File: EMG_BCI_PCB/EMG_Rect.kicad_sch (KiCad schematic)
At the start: 24 parts, among them U3D ADA4807-4, U4A ADA4807-4, U4B ADA4807-4, U4C ADA4807-4, U4D ADA4807-4, U4E ADA4807-4

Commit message: More schematic changes
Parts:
- removed TP6: TestPoint, Connector_PinHeader_2.54mm:PinHeader_1x01_P2.54mm_Vertical, symbol Connector:TestPoint
- removed U4C, U4D: ADA4807-4, Package_SO:TSSOP-14_4.4x5mm_P0.65mm, symbol EMG_Circuit:ADA4807-4
- added C5, C7: 4.7uF, Capacitor_SMD:C_0603_1608Metric_Pad1.05x0.95mm_HandSolder, symbol Device:C
- added R4, R5, R6: 10k, Resistor_SMD:R_0805_2012Metric_Pad1.15x1.40mm_HandSolder, symbol Device:R
- added unit 4 of U4
- added U8: MCP1501-18xCH, Package_TO_SOT_SMD:SOT-23-6, symbol Reference_Voltage:MCP1501-18xCH
- renumbered U4E to U4, U3D to U4, U4A to U4, U4B to U4
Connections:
- net +5V: now also C5.2, U8.4 (~{SHDN}), U8.6 (VDD)
- net Earth: now also C5.1, C7.1, U4.12 (+), U8.2 (GND), U8.3 (GND), U8.5 (GND)
- net LP_IN: now also U4.2 (-), R4.2; no longer U4.13 (-)
- net RectSignalAdc: now reaches C18.1, R17.1, TP5.1
- net at RV2.1, TP4.1: now also R17.2, U4.8; no longer U4.7
- net at R13.1, RV2.2: now also U4.9 (-); no longer U4.6 (-)
- net at R16.1, TP3.1: now also U4.10 (+), U4.7; no longer U4.1, U4.5 (+)
- net at C17.2, D1.1 (K), D2.2 (A): now also U4.1; no longer U4.14
- net at C17.1, D1.2 (A), R14.2: now also U4.3 (+); no longer U4.12 (+)
- net at D2.1 (K), R15.2: now also U4.6 (-); no longer U4.2 (-)
- net at R14.1, R16.2: now also U4.5 (+); no longer U4.3 (+)
- new net: C7.2, R6.2, U8.1 (OUT)
- new net: R4.1, R5.2, R6.1, U4.13 (-)
- new net RawSignalAdc: R5.1, U4.14
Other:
- moved on the sheet: C18, R17, TP5

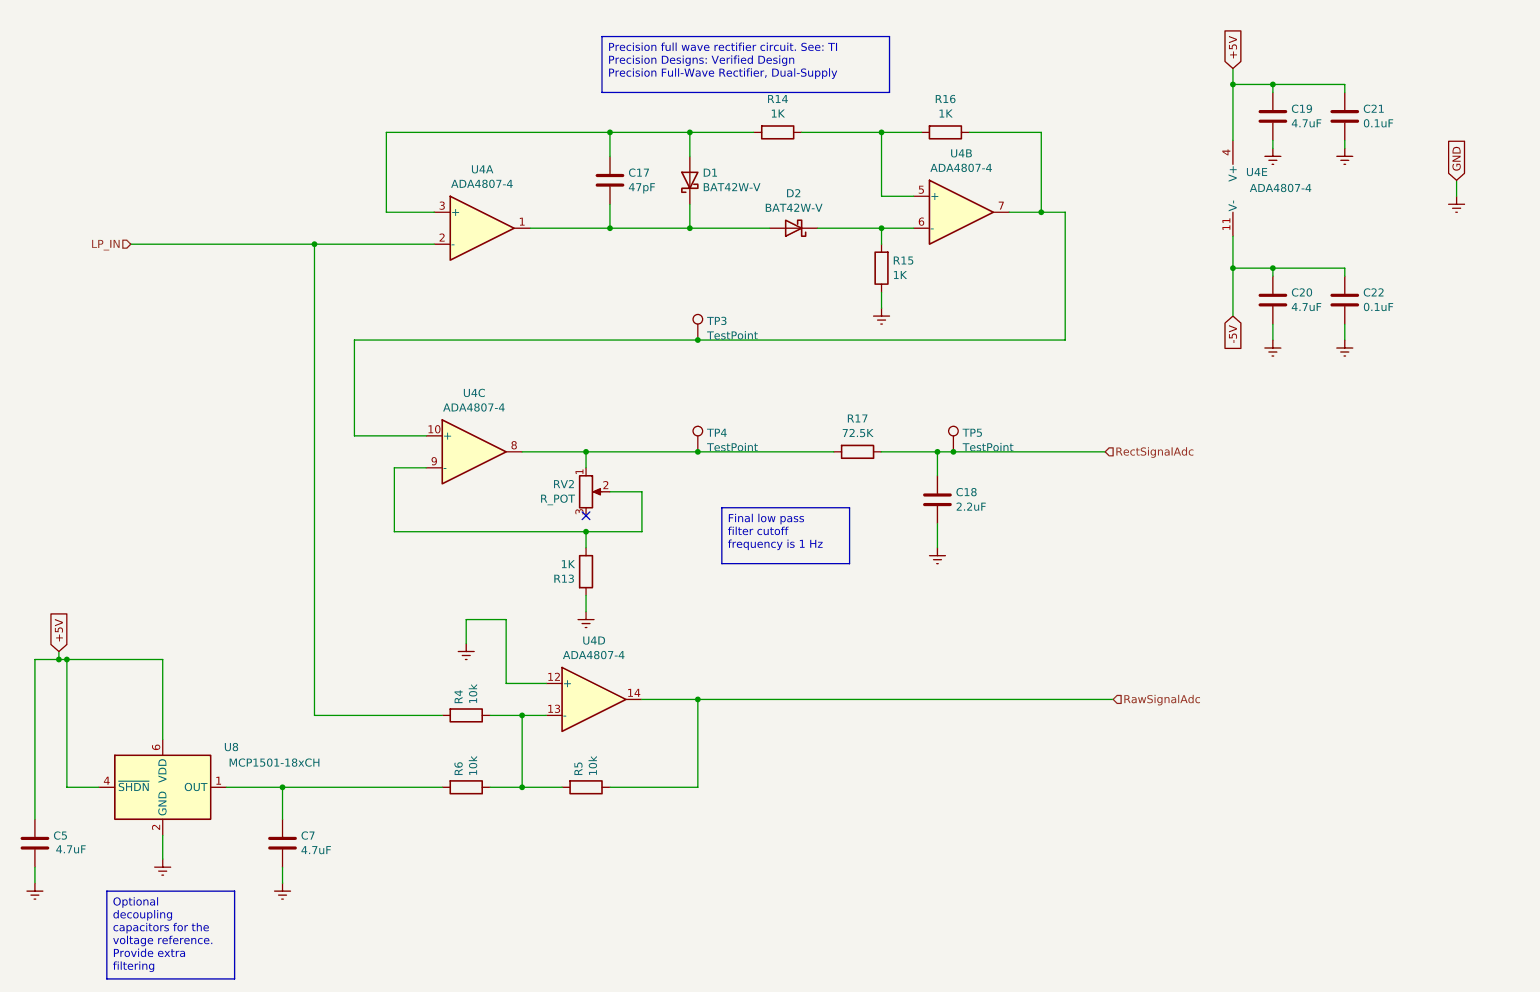
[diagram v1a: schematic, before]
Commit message: Added power symbols for +/-3.3V
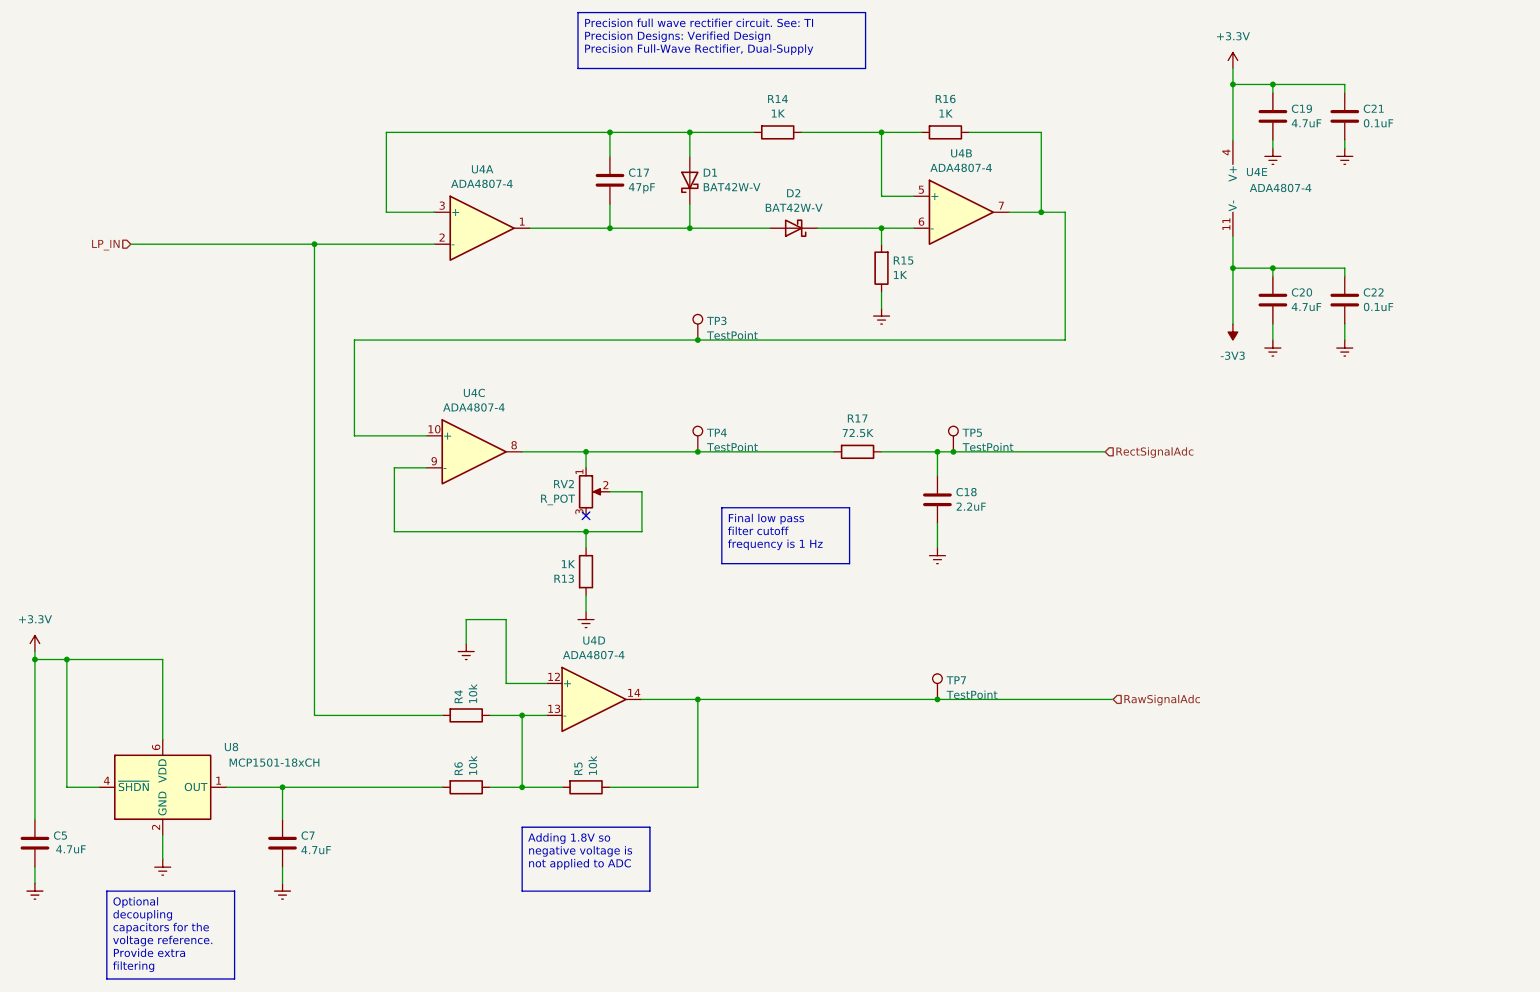
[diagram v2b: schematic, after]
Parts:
- added TP7: TestPoint, Connector_PinHeader_2.54mm:PinHeader_1x01_P2.54mm_Vertical, symbol Connector:TestPoint
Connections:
- net RawSignalAdc: now also TP7.1
- net +5V renamed +3.3V
- net -5V renamed -3V3

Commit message: Removed some warnings from the electrical rules
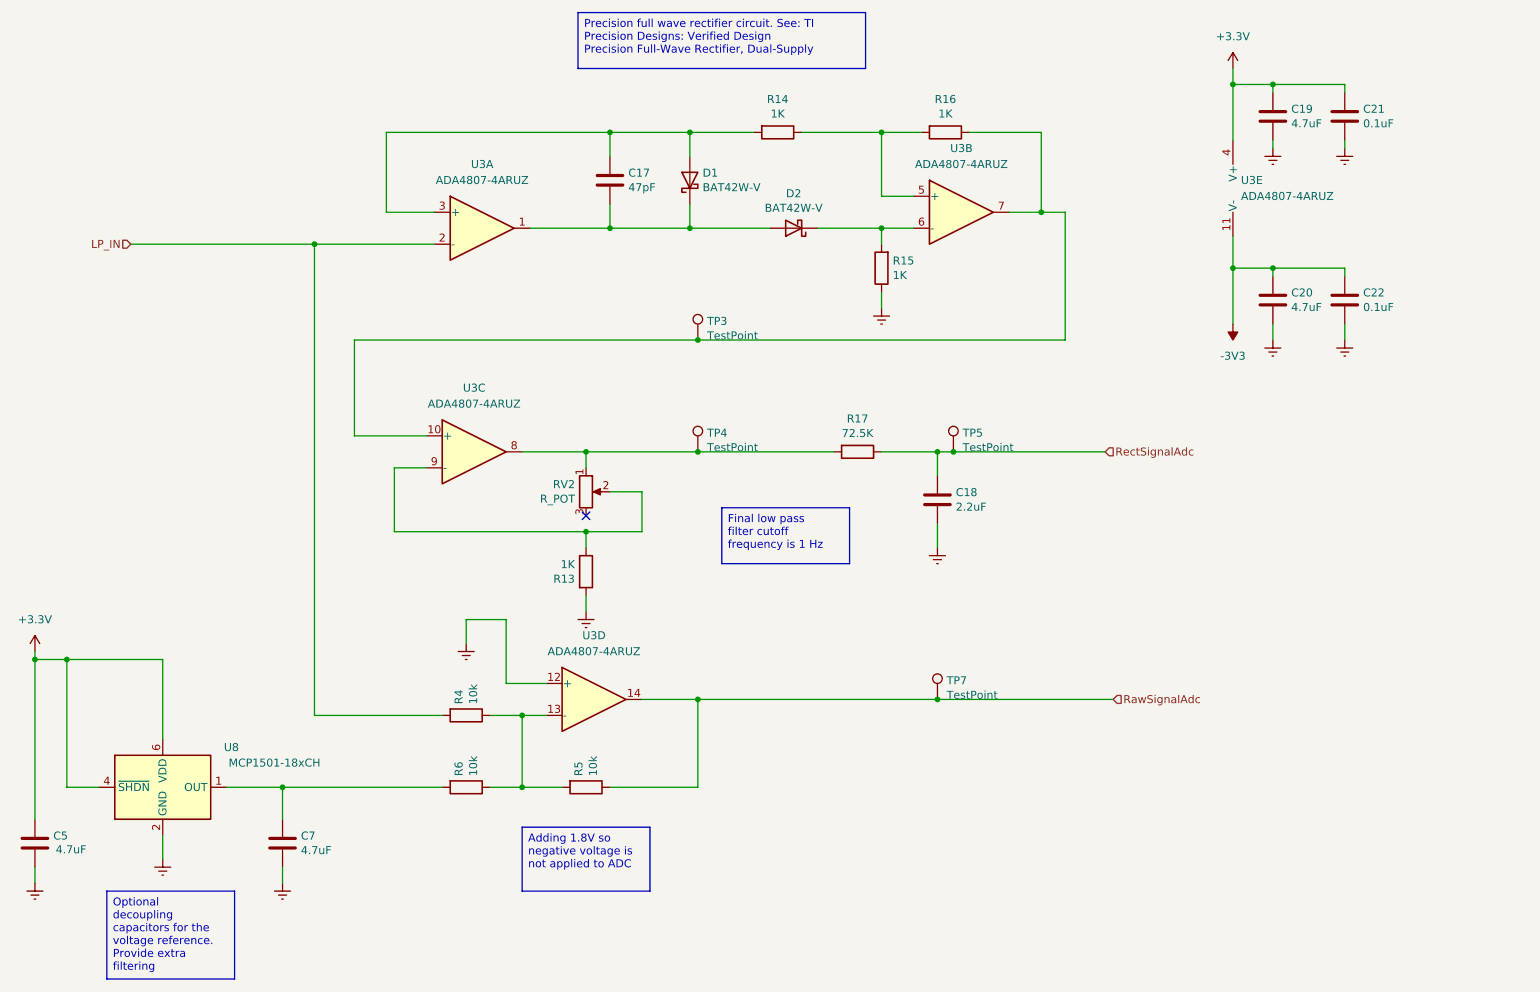
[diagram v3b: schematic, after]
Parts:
- removed U4: ADA4807-4, Package_SO:TSSOP-14_4.4x5mm_P0.65mm, symbol EMG_Circuit:ADA4807-4
- added U3: ADA4807-4ARUZ, Package_SO:TSSOP-14_4.4x5mm_P0.65mm, symbol Amplifier_Operational:ADA4807-4ARUZ
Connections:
- net +3.3V: now also U3.4 (V+)
- net -3V3: now also U3.11 (V-)
- net Earth: now also U3.12 (+)
- net LP_IN: now also U3.2 (-)
- net RawSignalAdc: now also U3.14
- net at R17.2, RV2.1, TP4.1: now also U3.8
- net at R13.1, RV2.2: now also U3.9 (-)
- net at R16.1, TP3.1: now also U3.10 (+), U3.7
- net at C17.2, D1.1 (K), D2.2 (A): now also U3.1
- net at C17.1, D1.2 (A), R14.2: now also U3.3 (+)
- net at D2.1 (K), R15.2: now also U3.6 (-)
- net at R14.1, R16.2: now also U3.5 (+)
- net at R4.1, R5.2, R6.1: now also U3.13 (-)
